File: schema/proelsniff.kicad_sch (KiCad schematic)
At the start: 60 parts, among them J1 USB_B_Micro, J2 Conn_01x05_Socket, J3 Screw_Terminal_01x02, J4 Screw_Terminal_01x02, J5 Conn_02x04_Odd_Even, J6 flat number selector, Q1 MMBT3904, Q2 MMBT3904, Q5 MMBT3904, Q6 MMBT5551L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

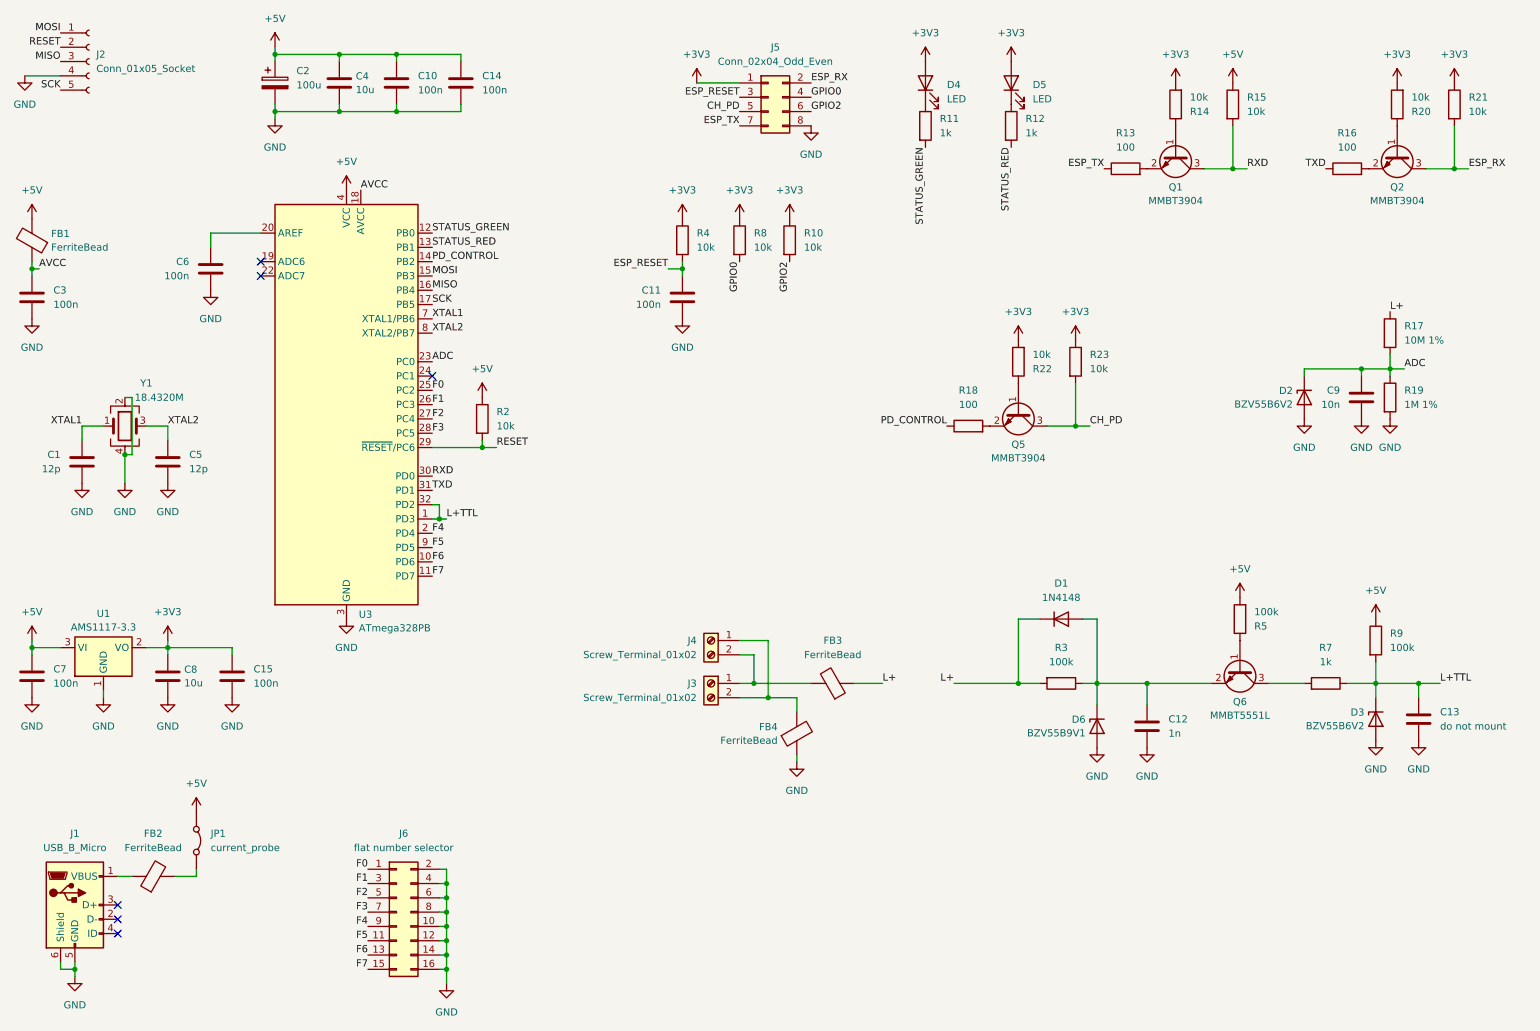
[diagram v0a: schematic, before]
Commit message: reorganize schematic
add connectivity and power management subsheets
add two GPIO signals from ESP-01
move line ADC to ADC7
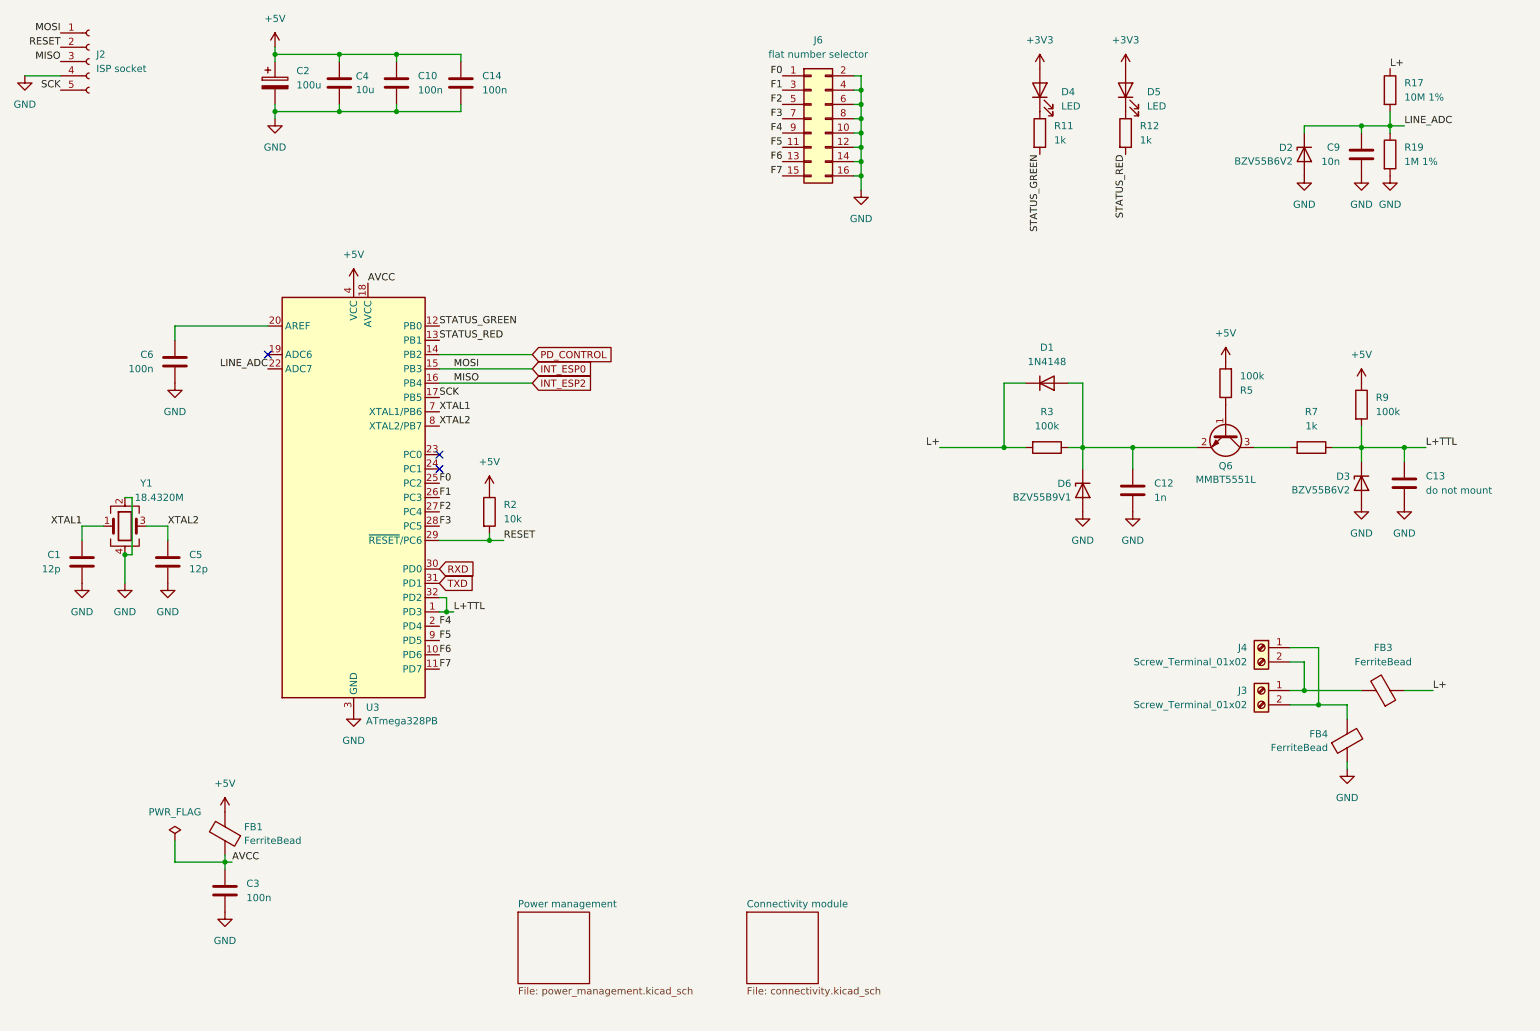
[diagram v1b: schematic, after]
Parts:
- removed C11, C15, C7: 100n, symbol Device:C
- removed C8: 10u, symbol Device:C
- removed FB2: FerriteBead, symbol Device:FerriteBead
- removed J1: USB_B_Micro, Connector_USB:USB_Micro-AB_Molex_47590-0001, symbol Connector:USB_B_Micro
- removed J5: Conn_02x04_Odd_Even, Connector_PinSocket_2.54mm:PinSocket_2x04_P2.54mm_Vertical, symbol Connector_Generic:Conn_02x04_Odd_Even
- removed JP1: current_probe, symbol Jumper:Jumper_2_Bridged
- removed Q1, Q2, Q5: MMBT3904, Package_TO_SOT_SMD:SOT-23, symbol Transistor_BJT:MMBT3904
- removed R10, R14, R15, R20, R21, R22, R23, R4, R8: 10k, symbol Device:R
- removed R13, R16, R18: 100, symbol Device:R
- removed U1: AMS1117-3.3, Package_TO_SOT_SMD:SOT-223-3_TabPin2, symbol Regulator_Linear:AMS1117-3.3
- J2: value Conn_01x05_Socket -> ISP socket
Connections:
- net LINE_ADC: now reaches U3.22 (ADC7)
- net LINE_ADC: now also C9.1, D2.1 (K), R17.2, R19.1
- removed net ADC: C9.1, D2.1 (K), R17.2, R19.1, U3.23 (PC0)
- net MISO renamed INT_ESP2
- net MOSI renamed INT_ESP0
- no-connect marks 6 -> 3
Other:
- added sheet Connectivity module (connectivity.kicad_sch)
- added sheet Power management (power_management.kicad_sch)
- moved on the sheet: C1, C12, C13, C3, C5, C6, C9, D1, D2, D3, D4, D5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

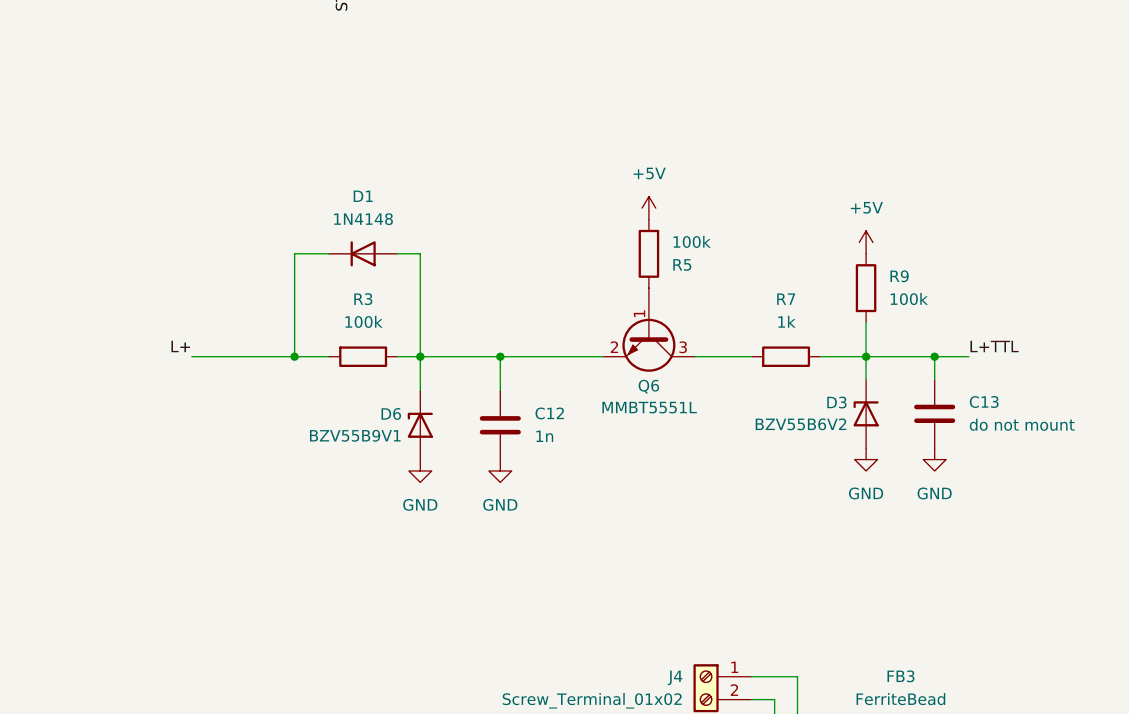
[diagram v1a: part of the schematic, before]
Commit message: redesign doorphone interface
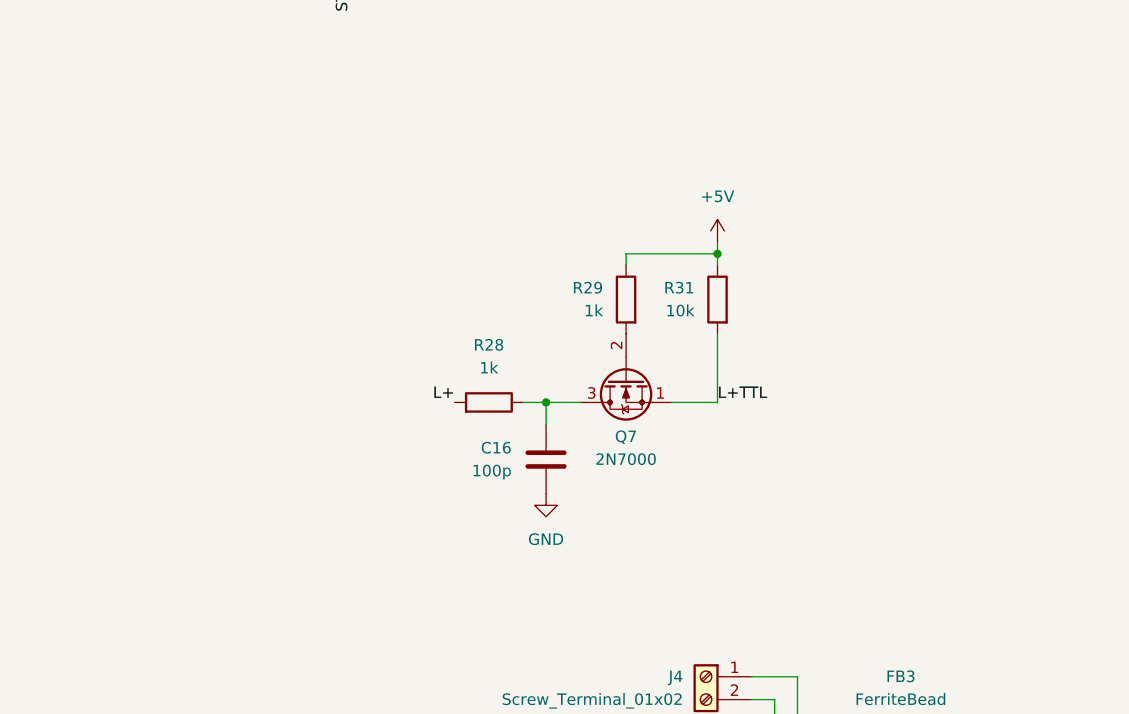
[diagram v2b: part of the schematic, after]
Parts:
- removed C12: 1n, symbol Device:C
- removed C13: do not mount, symbol Device:C
- removed D1: 1N4148, symbol Device:D
- removed D3: BZV55B6V2, Diode_SMD:D_MiniMELF, symbol Diode:BZV55B6V2
- removed D6: BZV55B9V1, Diode_SMD:D_MiniMELF, symbol Diode:BZV55B9V1
- removed Q6: MMBT5551L, Package_TO_SOT_SMD:SOT-23, symbol Transistor_BJT:MMBT5551L
- removed R3: 100k, Resistor_THT:R_Axial_DIN0207_L6.3mm_D2.5mm_P7.62mm_Horizontal, symbol Device:R
- removed R5, R9: 100k, symbol Device:R
- removed R7: 1k, symbol Device:R
- added C16: 100p, symbol Device:C
- added Q7: 2N7000, Package_TO_SOT_THT:TO-92_Inline, symbol Transistor_FET:2N7000
- added R28, R29: 1k, symbol Device:R
- added R31: 10k, symbol Device:R
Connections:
- net +5V: now also R29.1, R31.1
- net GND: now also C16.2
- net L+: now also R28.2
- net L+TTL: now also Q7.1 (S), R31.2
- new net: C16.1, Q7.3 (D), R28.1
- new net: Q7.2 (G), R29.2
